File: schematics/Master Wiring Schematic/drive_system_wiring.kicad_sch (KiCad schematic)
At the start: 8 parts, among them J10 Front Left Motor, J11 Conn_01x04, J12 Conn_01x04, J5 Rear Left Motor, J6 Conn_01x04, J7 Conn_01x04, J8 Front Right Motor, J9 Rear Right Motor

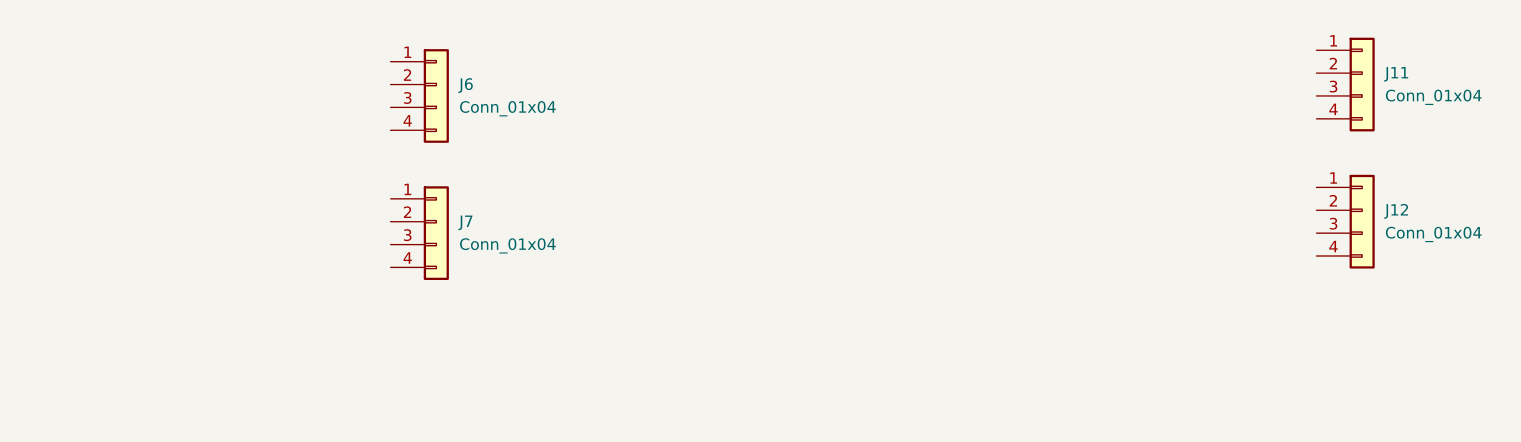
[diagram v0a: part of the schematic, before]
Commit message: Drive system components are being laid out on a subsheet
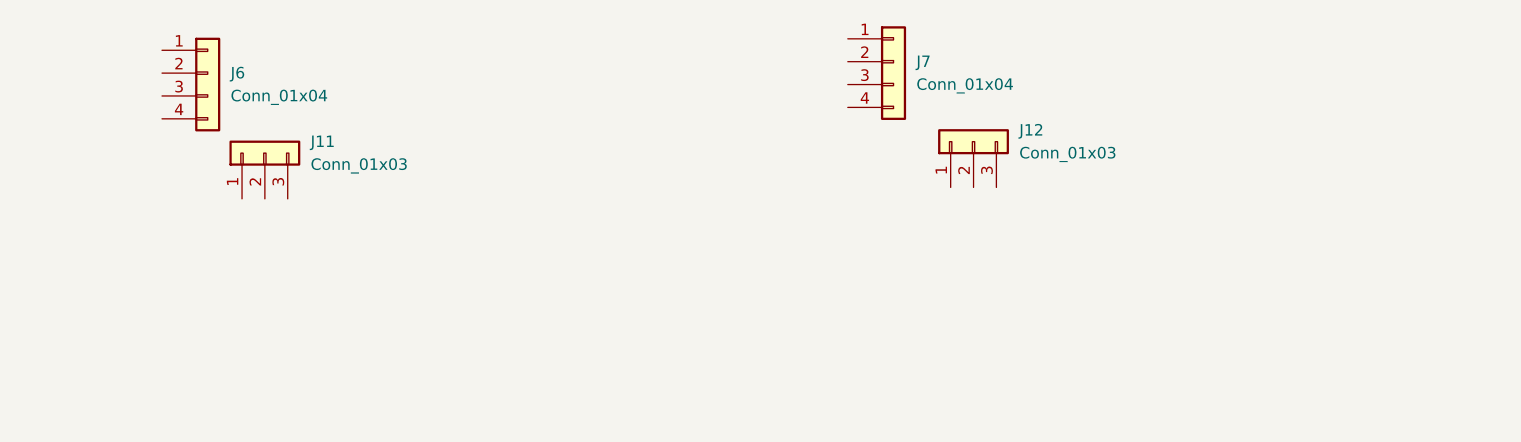
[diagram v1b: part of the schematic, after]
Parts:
- removed J11, J12: Conn_01x04, symbol Connector_Generic:Conn_01x04
- added J11, J12: Conn_01x03, symbol Connector_Generic:Conn_01x03
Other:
- moved on the sheet: J6

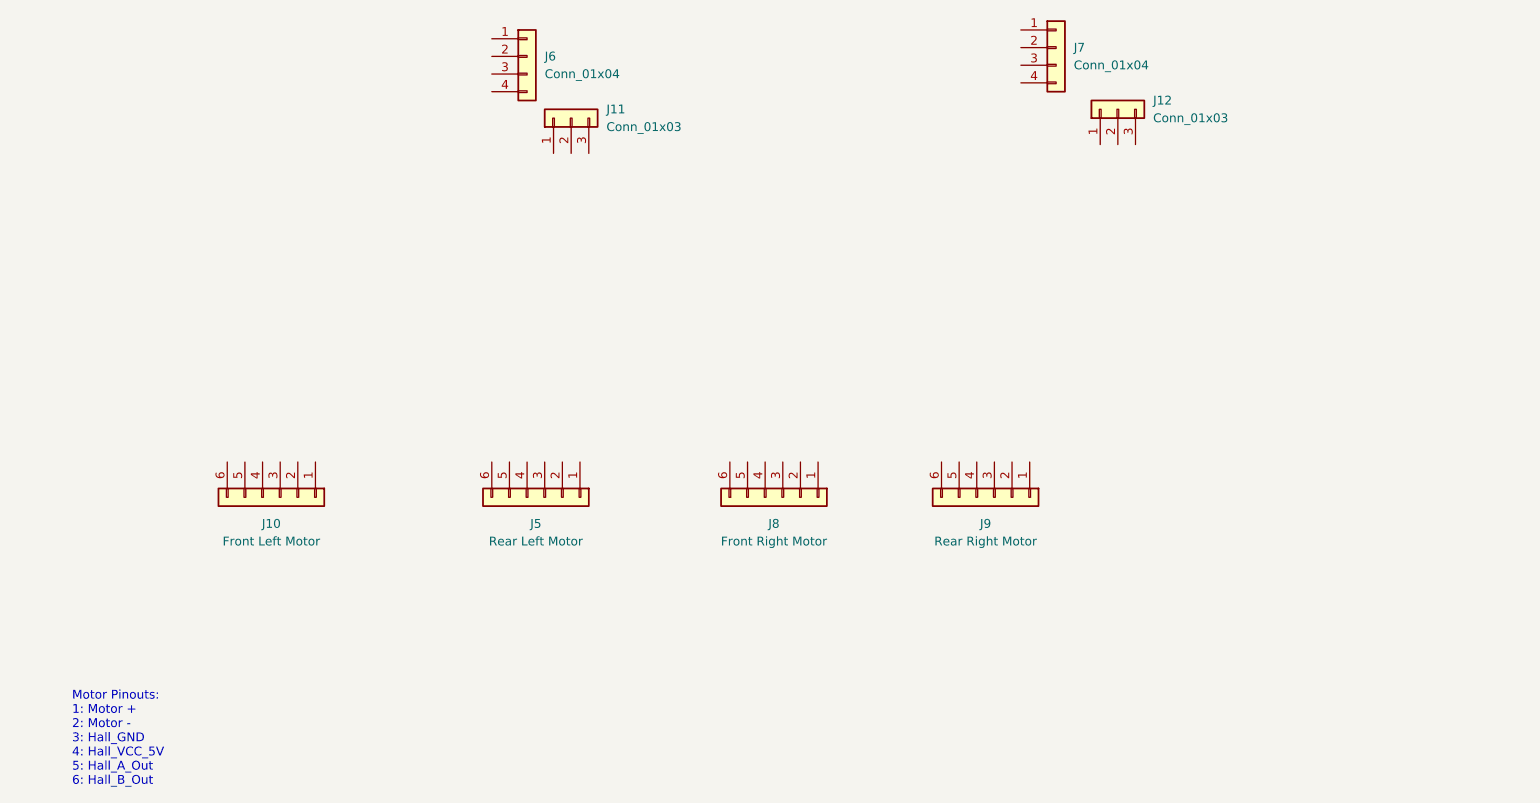
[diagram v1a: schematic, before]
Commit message: Drive system components are being laid out on a subsheet
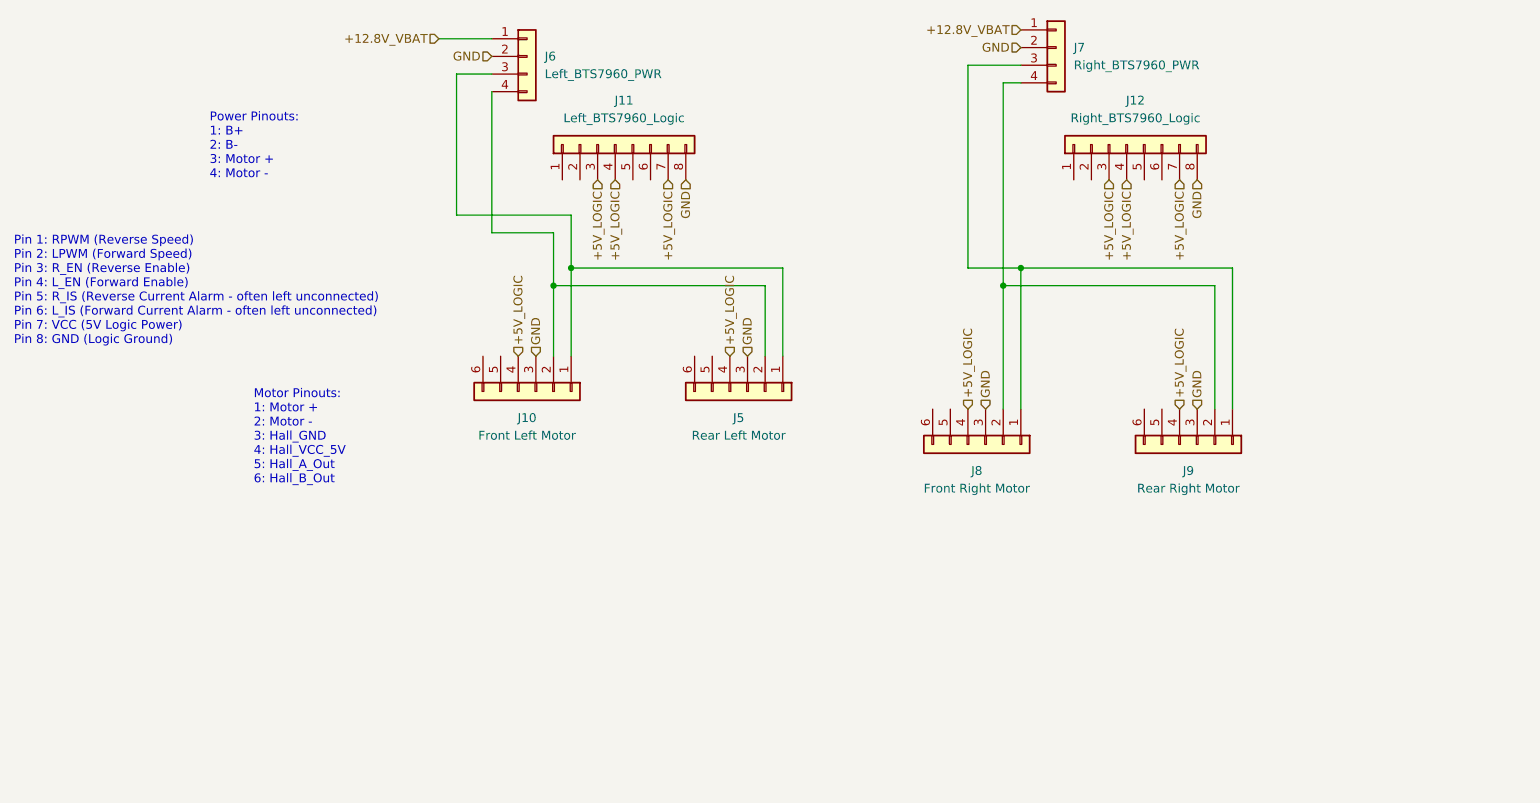
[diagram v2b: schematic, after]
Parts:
- removed J11, J12: Conn_01x03, symbol Connector_Generic:Conn_01x03
- added J11: Left_BTS7960_Logic, symbol Connector_Generic:Conn_01x08
- added J12: Right_BTS7960_Logic, symbol Connector_Generic:Conn_01x08
- J6: value Conn_01x04 -> Left_BTS7960_PWR
- J7: value Conn_01x04 -> Right_BTS7960_PWR
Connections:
- net +12.8V_VBAT: now reaches J7.1 (Pin_1)
- net +12.8V_VBAT: now also J6.1 (Pin_1)
- net GND: now reaches J7.2 (Pin_2)
- net GND: now also J10.3 (Pin_3), J5.3 (Pin_3), J6.2 (Pin_2), J8.3 (Pin_3), J9.3 (Pin_3), J11.8 (Pin_8), J12.8 (Pin_8)
- net at J7.3 (Pin_3): now also J8.1 (Pin_1), J9.1 (Pin_1)
- net at J7.4 (Pin_4): now also J8.2 (Pin_2), J9.2 (Pin_2)
- net +5V_LOGIC: now reaches J8.4 (Pin_4)
- net +5V_LOGIC: now also J10.4 (Pin_4), J5.4 (Pin_4), J9.4 (Pin_4), J11.3 (Pin_3), J11.4 (Pin_4), J11.7 (Pin_7), J12.3 (Pin_3), J12.4 (Pin_4), J12.7 (Pin_7)
- net at J5.1 (Pin_1): now also J10.1 (Pin_1), J6.3 (Pin_3)
- net at J5.2 (Pin_2): now also J10.2 (Pin_2), J6.4 (Pin_4)
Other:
- note added: "Pin 1: RPWM (Reverse Speed) Pin 2: LPWM (Forward Speed) Pin 3: R_EN (Reverse Enable) Pin 4: L_EN (Forward Enable) Pin 5: R_IS (Reverse Current Alarm - often left unconnected) Pin 6: L_IS (Forward Current Alarm - often left unconnected) Pin 7: VCC (5V Logic Power) Pin 8: GND (Logic Ground)"
- note added: "Power Pinouts: 1: B+ 2: B- 3: Motor + 4: Motor -"
- moved on the sheet: J10, J5, J8, J9

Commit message: Drive system components are being laid out on a subsheet
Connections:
- net FR_ENC_A: now reaches J8.5 (Pin_5)
- net FR_ENC_B: now reaches J8.6 (Pin_6)
- net RL_ENC_A: now reaches J5.5 (Pin_5)
- net RL_ENC_B: now reaches J5.6 (Pin_6)
- net LEFT_PWM_R: now reaches J11.1 (Pin_1)
- net LEFT_PWM_F: now reaches J11.2 (Pin_2)
- net RIGHT_PWM_R: now reaches J12.1 (Pin_1)
- net RIGHT_PWM_F: now reaches J12.2 (Pin_2)
- net RR_ENC_A: now reaches J9.5 (Pin_5)
- net RR_ENC_B: now reaches J9.6 (Pin_6)
- net FL_ENC_A: now reaches J10.5 (Pin_5)
- net FL_ENC_B: now reaches J10.6 (Pin_6)
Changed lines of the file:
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@@
+		)
+	)
+	(hierarchical_label "FR_ENC_B"
+		(shape output)
+		(at 152.4 125.73 90)
+		(effects
+			(font
+				(size 1.27 1.27)
+			)
+			(justify left)
 		)
 	)
@@
 		)
 	)
+	(hierarchical_label "RR_ENC_B"
+		(shape output)
+		(at 182.88 125.73 90)
+		(effects
+			(font
+				(size 1.27 1.27)
+			)
+			(justify left)
+		)
+	)
 	(hierarchical_label "GND"
 		(shape input)
@@
 		)
 	)
+	(hierarchical_label "RIGHT_PWM_R"
+		(shape input)
+		(at 172.72 92.71 270)
+		(effects
+			(font
+				(size 1.27 1.27)
+			)
+			(justify right)
+		)
+	)
 	(hierarchical_label "+5V_LOGIC"
 		(shape input)
@@
 		)
 	)
+	(hierarchical_label "RL_ENC_A"
+		(shape output)
+		(at 120.65 118.11 90)
+		(effects
+			(font
+				(size 1.27 1.27)
+			)
+			(justify left)
+		)
+	)
+	(hierarchical_label "LEFT_PWM_F"
+		(shape input)
+		(at 101.6 92.71 270)
+		(effects
+			(font
+				(size 1.27 1.27)
+			)
+			(justify right)
+		)
+	)
+	(hierarchical_label "FR_ENC_A"
+		(shape output)
+		(at 154.94 125.73 90)
+		(effects
+			(font
+				(size 1.27 1.27)
+			)
+			(justify left)
+		)
+	)
 	(hierarchical_label "+5V_LOGIC"
 		(shape input)
@@
 		)
 	)
+	(hierarchical_label "FL_ENC_B"
+		(shape output)
+		(at 87.63 118.11 90)
+		(effects
+			(font
+				(size 1.27 1.27)
+			)
+			(justify left)
+		)
+	)
 	(hierarchical_label "+5V_LOGIC"
 		(shape input)
@@
 		)
 	)
+	(hierarchical_label "RR_ENC_A"
+		(shape output)
+		(at 185.42 125.73 90)
+		(effects
+			(font
+				(size 1.27 1.27)
+			)
+			(justify left)
+		)
+	)
 	(hierarchical_label "GND"
 		(shape input)
@@
 		)
 	)
+	(hierarchical_label "LEFT_PWM_R"
+		(shape input)
+		(at 99.06 92.71 270)
+		(effects
+			(font
+				(size 1.27 1.27)
+			)
+			(justify right)
+		)
+	)
+	(hierarchical_label "RL_ENC_B"
+		(shape output)
+		(at 118.11 118.11 90)
+		(effects
+			(font
+				(size 1.27 1.27)
+			)
+			(justify left)
+		)
+	)
 	(hierarchical_label "+12.8V_VBAT"
 		(shape input)
@@
 		)
 	)
+	(hierarchical_label "FL_ENC_A"
+		(shape output)
+		(at 90.17 118.11 90)
+		(effects
+			(font
+				(size 1.27 1.27)
+			)
+			(justify left)
+		)
+	)
+	(hierarchical_label "RIGHT_PWM_F"
+		(shape input)
+		(at 175.26 92.71 270)
+		(effects
+			(font
+				(size 1.27 1.27)
+			)
+			(justify right)
+		)
+	)
